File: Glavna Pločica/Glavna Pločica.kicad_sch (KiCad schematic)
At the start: 19 parts, among them SW2 SW_Push, U1 ATMEGA328P-PU, U2 MCP23008-E_SS, U3 MCP4725xxx-xCH, U5 LM386, Y1 Crystal

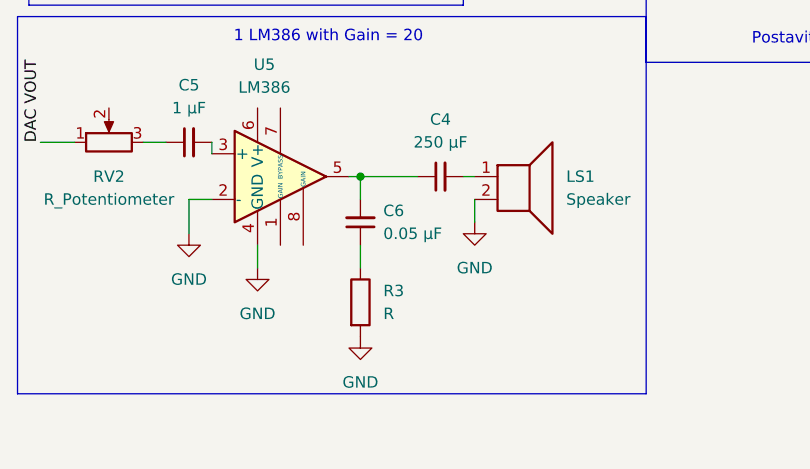
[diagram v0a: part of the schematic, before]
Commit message: Second push from laptop work
Removed RC filter
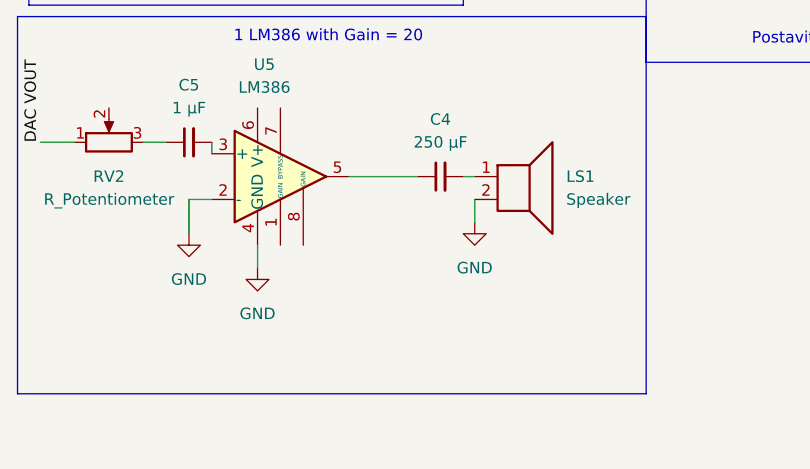
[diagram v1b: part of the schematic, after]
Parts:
- removed C6: 0.05 μF, symbol Device:C_Small
- removed R3: R, symbol Device:R
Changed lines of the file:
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@@
-	)
-	(junction
-		(at 104.14 95.25)
-		(diameter 0)
-		(color 0 0 0 0)
 	)
 	(junction
@@
 	(wire
 		(pts
-			(xy 104.14 95.25) (xy 110.49 95.25)
-		)
-		(stroke
-			(width 0)
-			(type default)
-		)
-	)
-	(wire
-		(pts
 			(xy 140.97 64.77) (xy 140.97 60.96)
 		)
@@
 	(wire
 		(pts
-			(xy 104.14 95.25) (xy 104.14 97.79)
-		)
-		(stroke
-			(width 0)
-			(type default)
-		)
-	)
-	(wire
-		(pts
 			(xy 156.21 64.77) (xy 140.97 64.77)
 		)
@@
 	(wire
 		(pts
-			(xy 104.14 102.87) (xy 104.14 105.41)
-		)
-		(stroke
-			(width 0)
-			(type default)
-		)
-	)
-	(wire
-		(pts
 			(xy 68.58 91.44) (xy 72.39 91.44)
 		)
@@
 	(wire
 		(pts
-			(xy 102.87 95.25) (xy 104.14 95.25)
-		)
-		(stroke
-			(width 0)
-			(type default)
-		)
-	)
-	(wire
-		(pts
 			(xy 151.13 35.56) (xy 153.67 35.56)
 		)
@@
 		(pts
 			(xy 21.59 115.57) (xy 21.59 118.11)
+		)
+		(stroke
+			(width 0)
+			(type default)
+		)
+	)
+	(wire
+		(pts
+			(xy 102.87 95.25) (xy 110.49 95.25)
 		)
 		(stroke
@@
 	)
 	(symbol
-		(lib_id "Device:C_Small")
-		(at 104.14 100.33 180)
-		(unit 1)
-		(exclude_from_sim no)
-		(in_bom yes)
-		(on_board yes)
-		(dnp no)
-		(fields_autoplaced yes)
-		(property "Reference" "C6"
-			(at 106.68 99.0535 0)
-			(effects
-				(font
-					(size 1.27 1.27)
-				)
-				(justify right)
-			)
-		)
-		(property "Value" "0.05 μF"
-			(at 106.68 101.5935 0)
-			(effects
-				(font
-					(size 1.27 1.27)
-				)
-				(justify right)
-			)
-		)
-		(property "Footprint" ""
-			(at 104.14 100.33 0)
-			(effects
-				(font
-					(size 1.27 1.27)
-				)
-				(hide yes)
-			)
-		)
-		(property "Datasheet" "~"
-			(at 104.14 100.33 0)
-			(effects
-				(font
-					(size 1.27 1.27)
-				)
-				(hide yes)
-			)
-		)
-		(property "Description" "Unpolarized capacitor, small symbol"
-			(at 104.14 100.33 0)
-			(effects
-				(font
-					(size 1.27 1.27)
-				)
-				(hide yes)
-			)
-		)
-		(pin "1"
-		)
-		(pin "2"
-		)
-		(instances
-			(project "Glavna Pločica"
-				(path "/2574e60a-000a-4854-9be3-da8ee196ecd1"
-					(reference "C6")
-					(unit 1)
-				)
-			)
-		)
-	)
-	(symbol
 		(lib_id "Display_Character:WC1602A")
 		(at 85.09 46.99 0)
@@
 	(symbol
 		(lib_id "power:GND")
-		(at 104.14 113.03 0)
-		(unit 1)
-		(exclude_from_sim no)
-		(in_bom yes)
-		(on_board yes)
-		(dnp no)
-		(fields_autoplaced yes)
-		(property "Reference" "#PWR09"
-			(at 104.14 119.38 0)
-			(effects
-				(font
-					(size 1.27 1.27)
-				)
-				(hide yes)
-			)
-		)
-		(property "Value" "GND"
-			(at 104.14 118.11 0)
-			(effects
-				(font
-					(size 1.27 1.27)
-				)
-			)
-		)
-		(property "Footprint" ""
-			(at 104.14 113.03 0)
-			(effects
-				(font
-					(size 1.27 1.27)
-				)
-				(hide yes)
-			)
-		)
-		(property "Datasheet" ""
-			(at 104.14 113.03 0)
-			(effects
-				(font
-					(size 1.27 1.27)
-				)
-				(hide yes)
-			)
-		)
-		(property "Description" "Power symbol creates a global label with name \"GND\" , ground"
-			(at 104.14 113.03 0)
-			(effects
-				(font
-					(size 1.27 1.27)
-				)
-				(hide yes)
-			)
-		)
-		(pin "1"
-		)
-		(instances
-			(project "Glavna Pločica"
-				(path "/2574e60a-000a-4854-9be3-da8ee196ecd1"
-					(reference "#PWR09")
-					(unit 1)
-				)
-			)
-		)
-	)
-	(symbol
-		(lib_id "power:GND")
 		(at 116.84 100.33 0)
 		(unit 1)
@@
 					(unit 1)
 				)
-			)
-		)
-	)
-	(symbol
-		(lib_id "Device:R")
-		(at 104.14 109.22 0)
-		(unit 1)
-		(exclude_from_sim no)
-		(in_bom yes)
-		(on_board yes)
-		(dnp no)
-		(fields_autoplaced yes)
-		(property "Reference" "R3"
-			(at 106.68 107.9499 0)
-			(effects
-				(font
-					(size 1.27 1.27)
-				)
-				(justify left)
-			)
-		)
-		(property "Value" "R"
-			(at 106.68 110.4899 0)
-			(effects
-				(font
-					(size 1.27 1.27)
-				)
-				(justify left)
-			)
-		)
-		(property "Footprint" ""
-			(at 102.362 109.22 90)
-			(effects
-				(font
-					(size 1.27 1.27)
-				)
-				(hide yes)
-			)
-		)
-		(property "Datasheet" "~"
-			(at 104.14 109.22 0)
-			(effects
-				(font
-					(size 1.27 1.27)
-				)
-				(hide yes)
-			)
-		)
-		(property "Description" "Resistor"
-			(at 104.14 109.22 0)
-			(effects
-				(font
-					(size 1.27 1.27)
-				)
-				(hide yes)
-			)
-		)
-		(pin "1"
-		)
-		(pin "2"
-		)
-		(instances
-			(project ""
-				(path "/2574e60a-000a-4854-9be3-da8ee196ecd1"
-					(reference "R3")
-					(unit 1)
-				)

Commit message: Promijena lm386 da moze G = 200
Ubačena trikondenzatora, jedan na ulaz pin 6 za čišće leveliranje zvuka, jedan između 1 i 8 kako bi dobili pojačanje 200 i jedan RC filter vraćen prije zvučnika
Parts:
- removed U2: MCP23008-E_SS, MCP23008-E_SS:SOP65P780X200-20N, symbol MCP23008-E_SS:MCP23008-E_SS
- added C6: 100nF, symbol Device:C_Small
- added C7: 10μF, symbol Device:C_Small
- added C8: 0.05 µF, symbol Device:C_Small
- added R7: 10K, symbol Device:R
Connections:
- net GND: now also R7.2
- net VCC: now also C6.1
- net at U5.1 (GAIN): now also C7.2
- net at C4.1, U5.5: now also C8.2
- net at U5.6 (V+): now also C6.2
- net at U5.8 (GAIN): now also C7.1
- new net: C8.1, R7.1
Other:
- note added: "0x60 5V to adress A0"
- note added: "1 LM386 with Gain = 200"
- note removed: "1 LM386 with Gain = 20"
- note removed: "Postavit cemo ga na 0x60 sa VCC na A0"
- moved on the sheet: C4, C5, LS1, RV2, U5
